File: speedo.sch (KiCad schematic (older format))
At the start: 43 parts, among them J1 Conn_01x08, J2 Conn_01x08, Q1 BSS138, SW1 SW_Push_Dual, SW2 SW_Push, U1 A1101ELHL, U2 LT1762, U3 4N25, U4 LT1762, U5 STM32F103C8Tx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

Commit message: Changed to atmel design
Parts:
- removed C19: 100nF, Capacitors_SMD:C_0603, symbol C
- removed SW1: SW_Push_Dual, symbol SW_Push_Dual
- removed SW2: SW_Push, symbol SW_Push
- removed SWD1: Conn_01x06, Pin_Headers:Pin_Header_Straight_1x06_Pitch1.27mm, symbol Conn_01x06
- removed U5: STM32F103C8Tx, Housings_QFP:LQFP-48_7x7mm_Pitch0.5mm, symbol STM32F103C8Tx
- added C19: 10uF, Capacitors_Tantalum_SMD:CP_Tantalum_Case-A_EIA-3216-18_Reflow, symbol CP
- added J3: Prog Header, Pin_Headers:Pin_Header_Straight_2x03_Pitch2.54mm, symbol Conn_02x03_Counter_Clockwise
- added L1: 10uH, Inductors_SMD:L_1206, symbol L
- added R10, R11: 1K, Resistors_SMD:R_0603, symbol R
- added R9: 10K, Resistors_SMD:R_0603, symbol R
- added SW1: SW_Push, custom_footprint:switch-kpt-1187B-SMD, symbol SW_Push
- added U5: ATMEGA644-20AU, Housings_QFP:TQFP-44-1EP_10x10mm_Pitch0.8mm, symbol ATMEGA644-20AU
- C1: value C -> 100nF
- C11, C6: value C -> 10nF
- C14: value 100nF -> 10nF
- C2: value C -> 4.7nF
- C5: value C -> 1nF
- J1, J2: footprint Pin_Headers:Pin_Header_Straight_1x08_Pitch2.54mm -> Connectors_Molex:Molex_KK-6410-08_08x2.54mm_Straight
- R1: footprint Resistors_THT:R_Axial_Power_L25.0mm_W9.0mm_P7.62mm_Vertical -> Resistors_SMD:R_1206
- R2, R3, R5, R7: value R -> 10K
- R4: value R -> 4.7K
- R6: value R -> 100K
- U1: value A1101ELHL -> US1881; footprint TO_SOT_Packages_SMD:SOT-23 -> custom_footprint:TO-92-pins-3-in-a-row
- U2: value LT1762 -> LT1762-3.3
- U3: footprint Housings_DIP:DIP-6_W7.62mm -> custom_footprint:4N2X
- U4: value LT1762 -> LT1762-5
- Y1: value Crystal -> 10MHz 18pF
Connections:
- net labels added: MISO, RX, Reset, TX
- net labels removed: BOOT0, GNDA, NRST, SWCLK, SWDIO, SWO
- wire segments 112 -> 109
- no-connect marks 26 -> 2
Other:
- note removed: "LT1762-3.3"
- note removed: "LT1762-5"
- moved on the sheet: C1, C10, C11, C12, C13, C14, C15, C16, C17, C2, C3, C4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

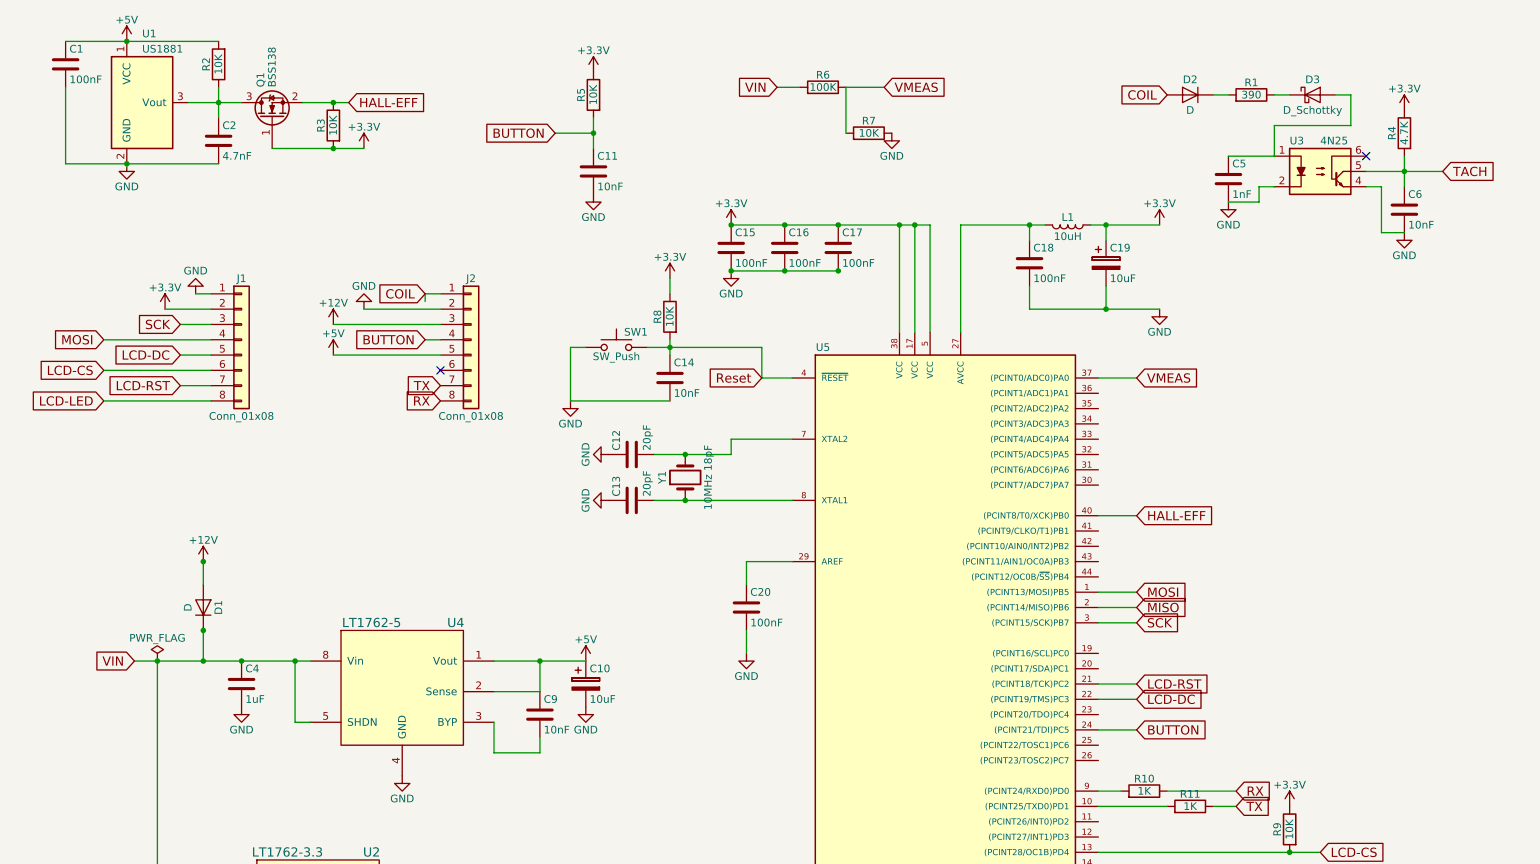
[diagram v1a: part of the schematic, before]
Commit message: Removed traces, redid placement
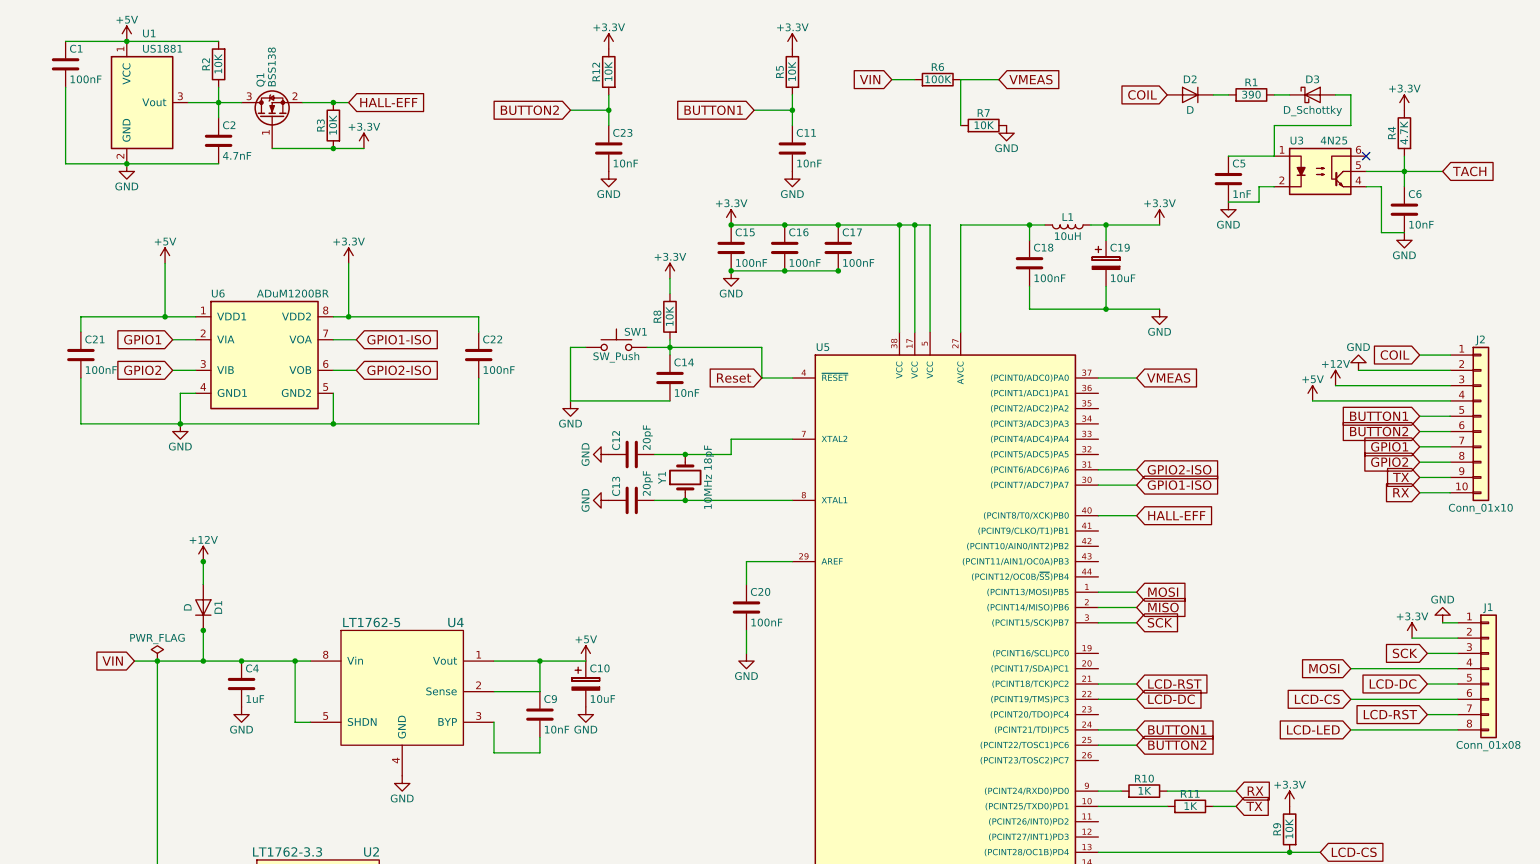
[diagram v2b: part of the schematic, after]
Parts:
- removed J2: Conn_01x08, Connectors_Molex:Molex_KK-6410-08_08x2.54mm_Straight, symbol Conn_01x08
- added C21, C22: 100nF, Capacitors_SMD:C_0603, symbol C
- added C23: 10nF, Capacitors_SMD:C_0603, symbol C
- added J2: Conn_01x10, Connectors_Molex:Molex_PicoBlade_53047-1010_10x1.25mm_Straight, symbol Conn_01x10
- added R12: 10K, Resistors_SMD:R_0603, symbol R
- added U6: ADuM1200BR, Housings_SOIC:SOIC-8_3.9x4.9mm_Pitch1.27mm, symbol ADuM1200BR
- J1: footprint Connectors_Molex:Molex_KK-6410-08_08x2.54mm_Straight -> Connectors_Molex:Molex_PicoBlade_53047-0810_08x1.25mm_Straight
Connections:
- net +12V: now also J2.3 (Pin_3)
- net +3V3: now also C22.1, R12.1, U6.8 (VDD2)
- net +5V: now also C21.1, J2.4 (Pin_4), U6.1 (VDD1)
- net COIL: now also J2.1 (Pin_1)
- net GND: now also C21.2, C22.2, C23.2, J2.2 (Pin_2), U6.4 (GND1), U6.5 (GND2)
- net RX: now also J2.10 (Pin_10)
- net TX: now also J2.9 (Pin_9)
- net BUTTON2: now reaches U5.25 ((PCINT22/TOSC1)PC6)
- net BUTTON2: now also C23.1, J2.6 (Pin_6), R12.2
- net GPIO1-ISO: now reaches U5.30 ((PCINT7/ADC7)PA7)
- net GPIO1-ISO: now also U6.7 (VOA)
- net GPIO2-ISO: now reaches U5.31 ((PCINT6/ADC6)PA6)
- net GPIO2-ISO: now also U6.6 (VOB)
- net BUTTON renamed BUTTON1
- net BUTTON1: now also J2.5 (Pin_5)
- new net GPIO1: J2.7 (Pin_7), U6.2 (VIA)
- new net GPIO2: J2.8 (Pin_8), U6.3 (VIB)
- no-connect marks 2 -> 1
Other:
- moved on the sheet: C11, J1, R5, R6, R7

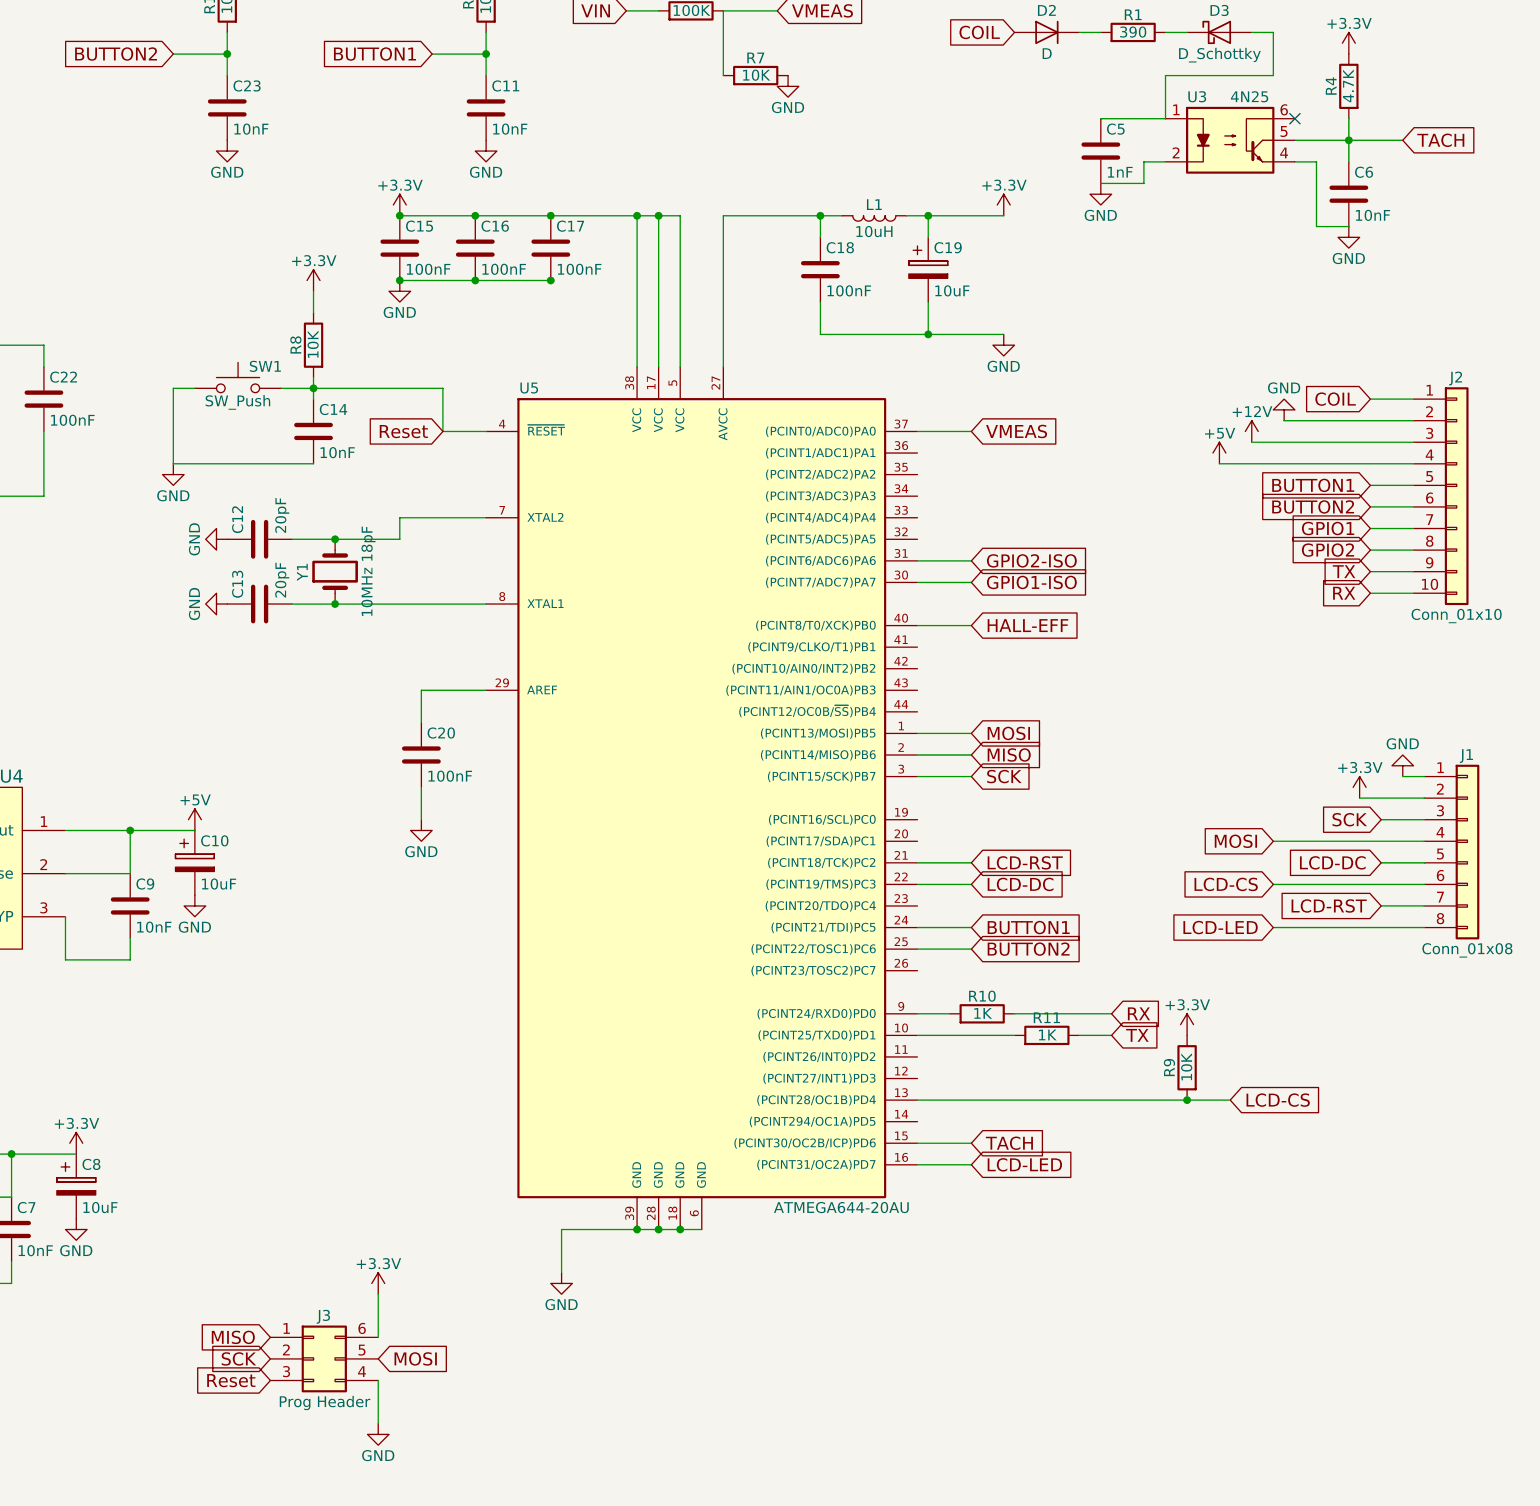
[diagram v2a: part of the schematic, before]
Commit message: changed atmega644 to atmega328
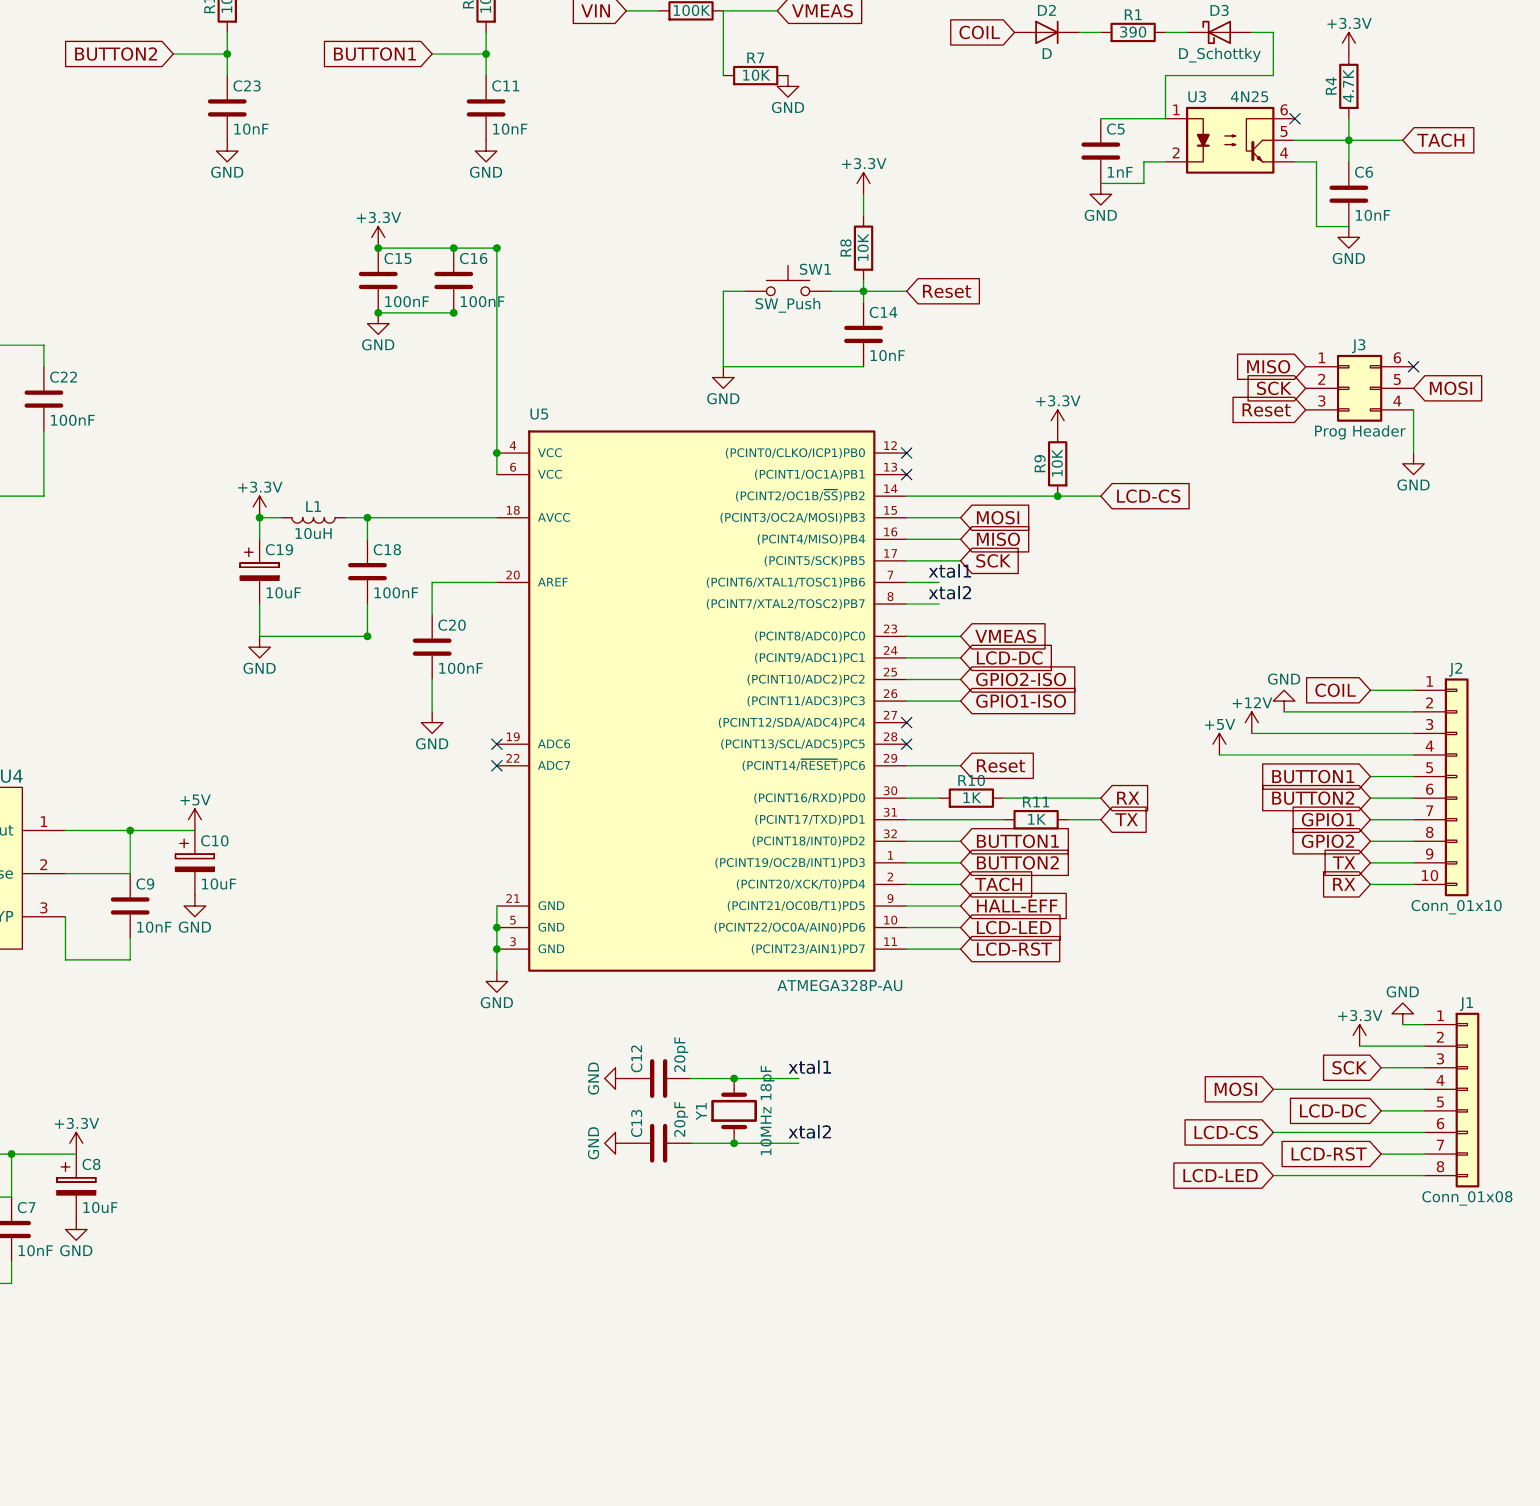
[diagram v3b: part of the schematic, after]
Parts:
- removed C17: 100nF, Capacitors_SMD:C_0603, symbol C
- removed U5: ATMEGA644-20AU, Housings_QFP:TQFP-44-1EP_10x10mm_Pitch0.8mm, symbol ATMEGA644-20AU
- added U5: ATMEGA328P-AU, Housings_QFP:TQFP-32_7x7mm_Pitch0.8mm, symbol ATMEGA328P-AU
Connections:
- net +3V3: now also L1.2, U5.4 (VCC), U5.6 (VCC); no longer J3.6 (Pin_6), L1.1
- net BUTTON1: now also U5.32 ((PCINT18/INT0)PD2)
- net BUTTON2: now also U5.1 ((PCINT19/OC2B/INT1)PD3)
- net GND: now also U5.21 (GND), U5.3 (GND), U5.5 (GND)
- net GPIO1-ISO: now also U5.26 ((PCINT11/ADC3)PC3)
- net GPIO2-ISO: now also U5.25 ((PCINT10/ADC2)PC2)
- net HALL-EFF: now also U5.9 ((PCINT21/OC0B/T1)PD5)
- net LCD-CS: now also U5.14 ((PCINT2/OC1B/~SS~)PB2)
- net LCD-DC: now also U5.24 ((PCINT9/ADC1)PC1)
- net LCD-LED: now also U5.10 ((PCINT22/OC0A/AIN0)PD6)
- net LCD-RST: now also U5.11 ((PCINT23/AIN1)PD7)
- net MISO: now also U5.16 ((PCINT4/MISO)PB4)
- net MOSI: now also U5.15 ((PCINT3/OC2A/MOSI)PB3)
- net Reset: now also U5.29 ((PCINT14/~RESET~)PC6)
- net SCK: now also U5.17 ((PCINT5/SCK)PB5)
- net TACH: now also U5.2 ((PCINT20/XCK/T0)PD4)
- net VMEAS: now also U5.23 ((PCINT8/ADC0)PC0)
- net xtal2: now reaches C13.2, Y1.1
- net xtal2: now also U5.8 ((PCINT7/XTAL2/TOSC2)PB7)
- net xtal1: now reaches C12.2, Y1.2
- net xtal1: now also U5.7 ((PCINT6/XTAL1/TOSC1)PB6)
- net at R11.2: now also U5.31 ((PCINT17/TXD)PD1)
- net at C18.1: now also L1.1, U5.18 (AVCC); no longer L1.2
- net at C20.1: now also U5.20 (AREF)
- net at R10.2: now also U5.30 ((PCINT16/RXD)PD0)
- no-connect marks 1 -> 8
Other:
- moved on the sheet: C12, C13, C14, C15, C16, C18, C19, C20, J1, J2, J3, L1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

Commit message: Fixed footprints
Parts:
- J1: footprint Connectors_Molex:Molex_PicoBlade_53047-0810_08x1.25mm_Straight -> Connectors_Molex:Molex_PicoBlade_53398-0871_08x1.25mm_Straight
- J2: footprint Connectors_Molex:Molex_PicoBlade_53047-1010_10x1.25mm_Straight -> Connectors_Molex:Molex_PicoBlade_53398-1071_10x1.25mm_Straight
- U2, U4: footprint Housings_SSOP:MSOP-8-1EP_3x3mm_Pitch0.65mm -> Housings_SSOP:MSOP-8_3x3mm_Pitch0.65mm
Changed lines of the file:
@@
 F 0 "U2" H 2800 6950 60  0000 C CNN
 F 1 "LT1762-3.3" H 2250 6950 60  0000 C CNN
-F 2 "Housings_SSOP:MSOP-8-1EP_3x3mm_Pitch0.65mm" H 2450 6500 60  0001 C CNN
+F 2 "Housings_SSOP:MSOP-8_3x3mm_Pitch0.65mm" H 2450 6500 60  0001 C CNN
 F 3 "" H 2450 6500 60  0001 C CNN
 	1    2450 6500
@@
 F 0 "U4" H 3350 5450 60  0000 C CNN
 F 1 "LT1762-5" H 2800 5450 60  0000 C CNN
-F 2 "Housings_SSOP:MSOP-8-1EP_3x3mm_Pitch0.65mm" H 3000 5000 60  0001 C CNN
+F 2 "Housings_SSOP:MSOP-8_3x3mm_Pitch0.65mm" H 3000 5000 60  0001 C CNN
 F 3 "" H 3000 5000 60  0001 C CNN
 	1    3000 5000
@@
 F 0 "J1" H 10100 6400 50  0000 C CNN
 F 1 "Conn_01x08" H 10100 5500 50  0000 C CNN
-F 2 "Connectors_Molex:Molex_PicoBlade_53047-0810_08x1.25mm_Straight" H 10100 6000 50  0001 C CNN
+F 2 "Connectors_Molex:Molex_PicoBlade_53398-0871_08x1.25mm_Straight" H 10100 6000 50  0001 C CNN
 F 3 "" H 10100 6000 50  0001 C CNN
 	1    10100 6000
@@
 F 0 "J2" H 10050 5050 50  0000 C CNN
 F 1 "Conn_01x10" H 10050 3950 50  0000 C CNN
-F 2 "Connectors_Molex:Molex_PicoBlade_53047-1010_10x1.25mm_Straight" H 10050 4550 50  0001 C CNN
+F 2 "Connectors_Molex:Molex_PicoBlade_53398-1071_10x1.25mm_Straight" H 10050 4550 50  0001 C CNN
 F 3 "" H 10050 4550 50  0001 C CNN
 	1    10050 4550
